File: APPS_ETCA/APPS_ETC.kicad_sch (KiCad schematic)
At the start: 7 parts, among them U1 NUCLEO-L432KC, U2 ISO1050DUB, U3 A1365xKTTN-1, U4 A1365xKTTN-1, U5 L78S05CV

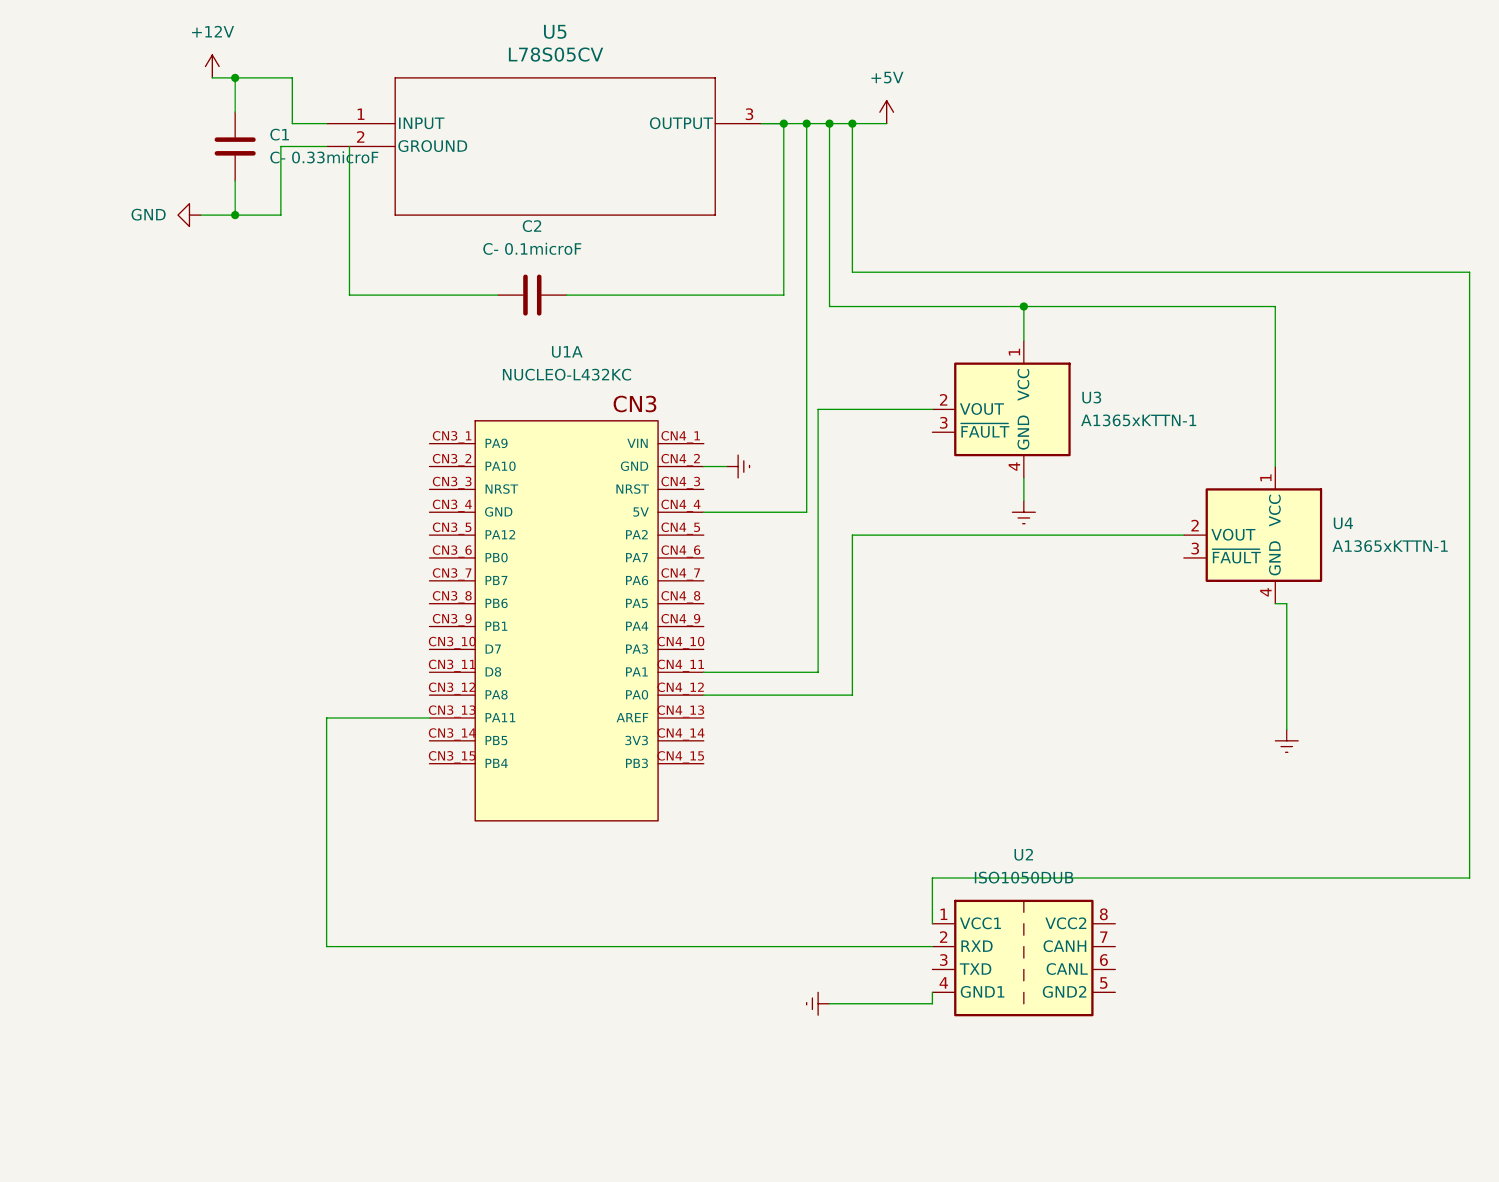
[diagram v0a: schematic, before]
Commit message: schema 3/4 done - need connectors in place of HE
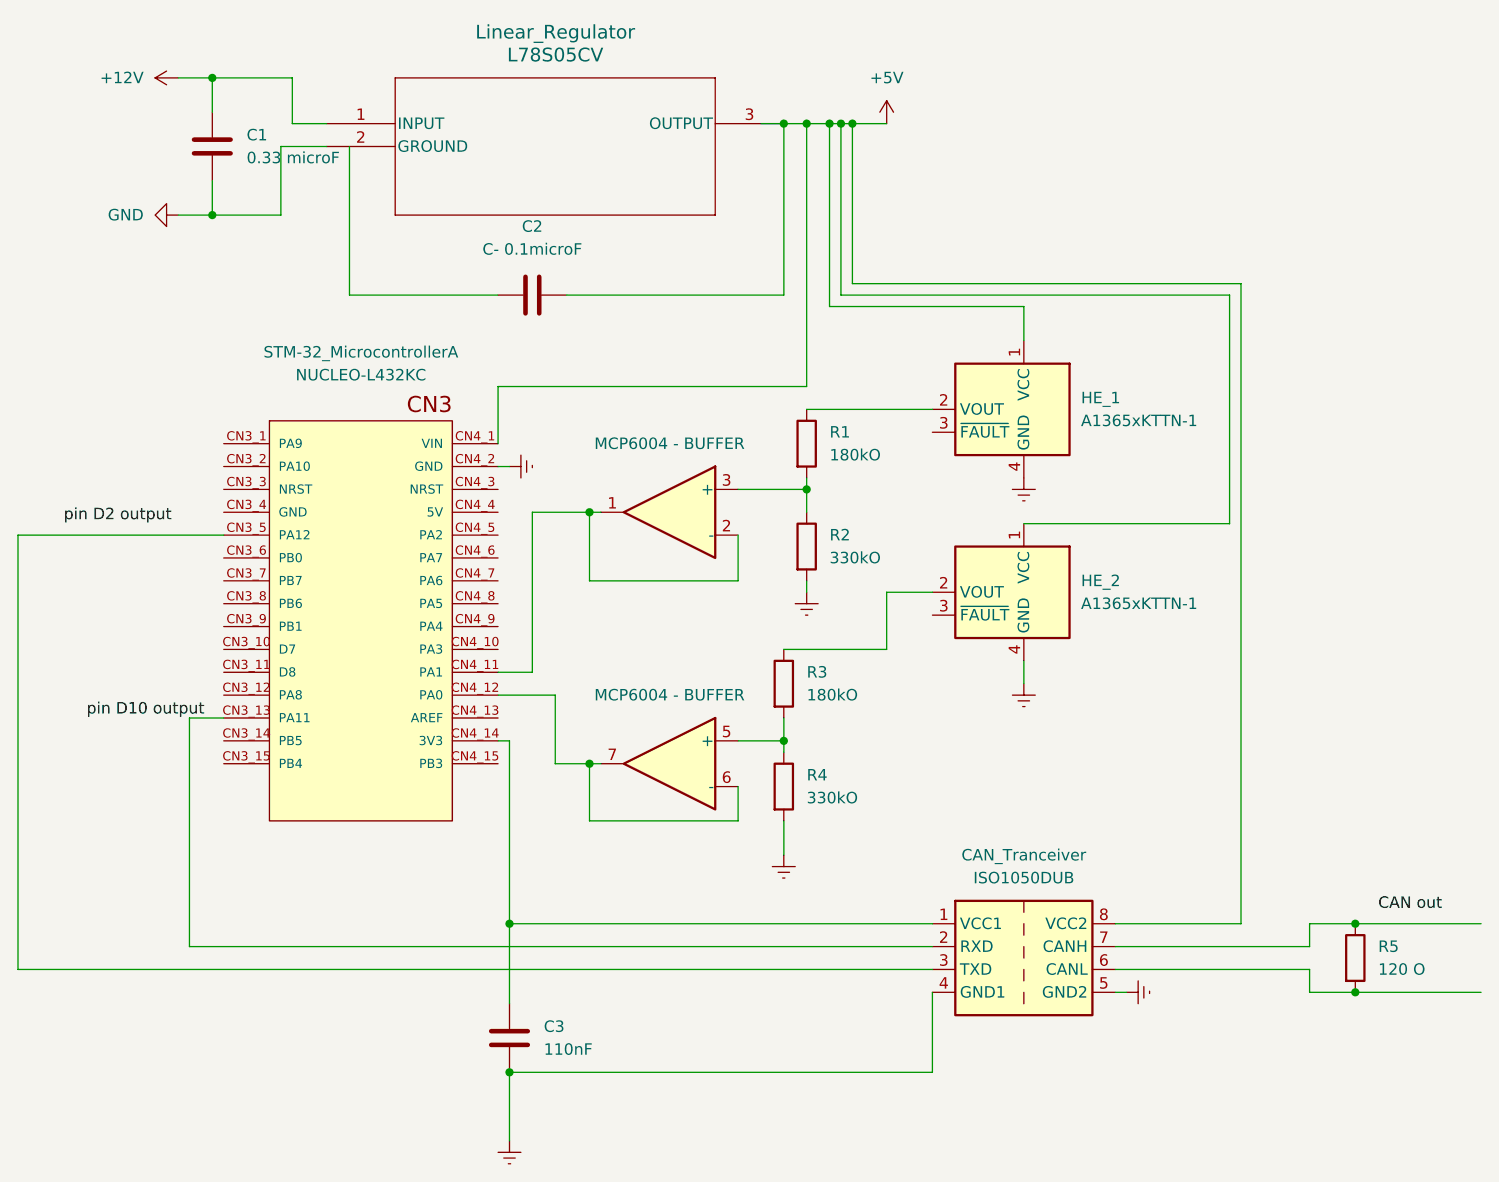
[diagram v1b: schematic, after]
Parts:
- added C3: 110nF, symbol Device:C
- added R1, R3: 180kO, symbol Device:R
- added R2, R4: 330kO, symbol Device:R
- added R5: 120 O, symbol Device:R
- added U6: MCP6004 - BUFFER, symbol Amplifier_Operational:MCP6004
- C1: value C- 0.33microF -> 0.33 microF
- renumbered U2 to CAN_Tranceiver, U3 to HE_1, U4 to HE_2, U5 to Linear_Regulator, U1 to STM-32_Microcontroller
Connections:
- net +5V: now also CAN_Tranceiver.8 (VCC2), STM-32_Microcontroller.CN4_1 (VIN); no longer CAN_Tranceiver.1 (VCC1), STM-32_Microcontroller.CN4_4 (5V)
- net Earth: now also CAN_Tranceiver.5 (GND2), C3.2, R2.2, R4.2
- net at HE_1.2 (VOUT): now also R1.1; no longer STM-32_Microcontroller.CN4_11 (PA1)
- net at STM-32_Microcontroller.CN3_5 (PA12): now also CAN_Tranceiver.3 (TXD)
- net at HE_2.2 (VOUT): now also R3.1; no longer STM-32_Microcontroller.CN4_12 (PA0)
- net at STM-32_Microcontroller.CN4_14 (3V3): now also CAN_Tranceiver.1 (VCC1), C3.1
- net at CAN_Tranceiver.6 (CANL): now also R5.2
- net at CAN_Tranceiver.7 (CANH): now also R5.1
- new net: R3.2, R4.1, U6.5 (+)
- new net: STM-32_Microcontroller.CN4_12 (PA0), U6.6 (-), U6.7
- new net: R1.2, R2.1, U6.3 (+)
- new net: STM-32_Microcontroller.CN4_11 (PA1), U6.1, U6.2 (-)
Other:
- moved on the sheet: C1, HE_2, STM-32_MicrocontrollerA

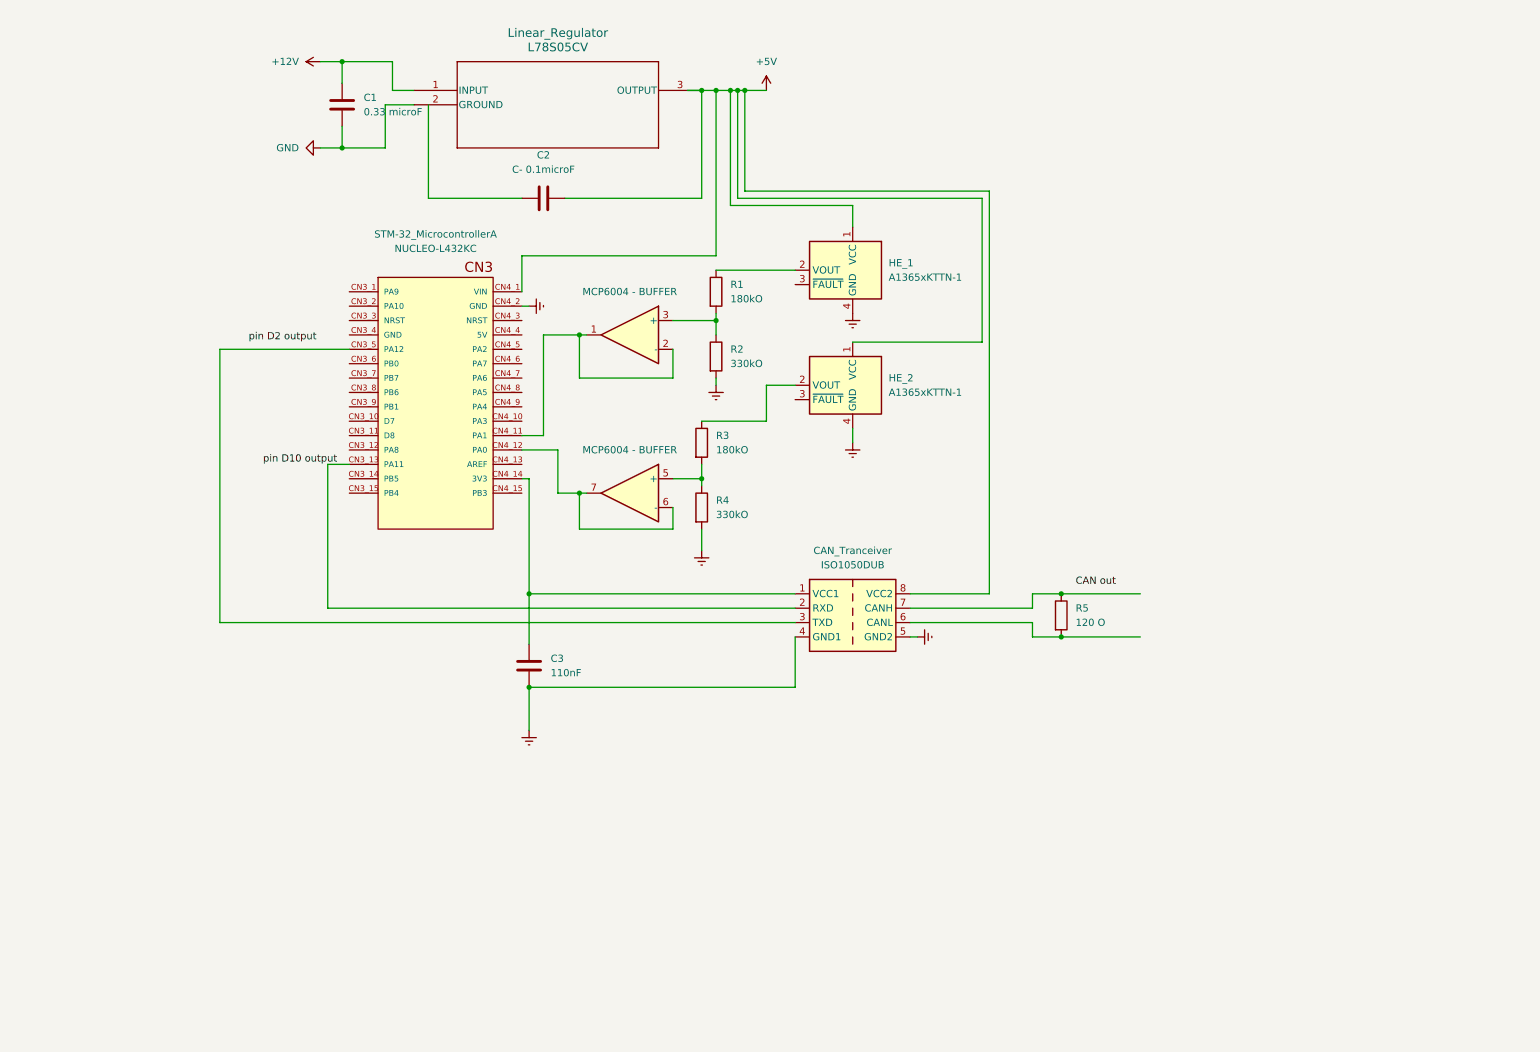
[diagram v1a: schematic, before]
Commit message: Added footprints for enclosure connector Add RTDS and TSAL Control Circuit. Add enclosure connections.
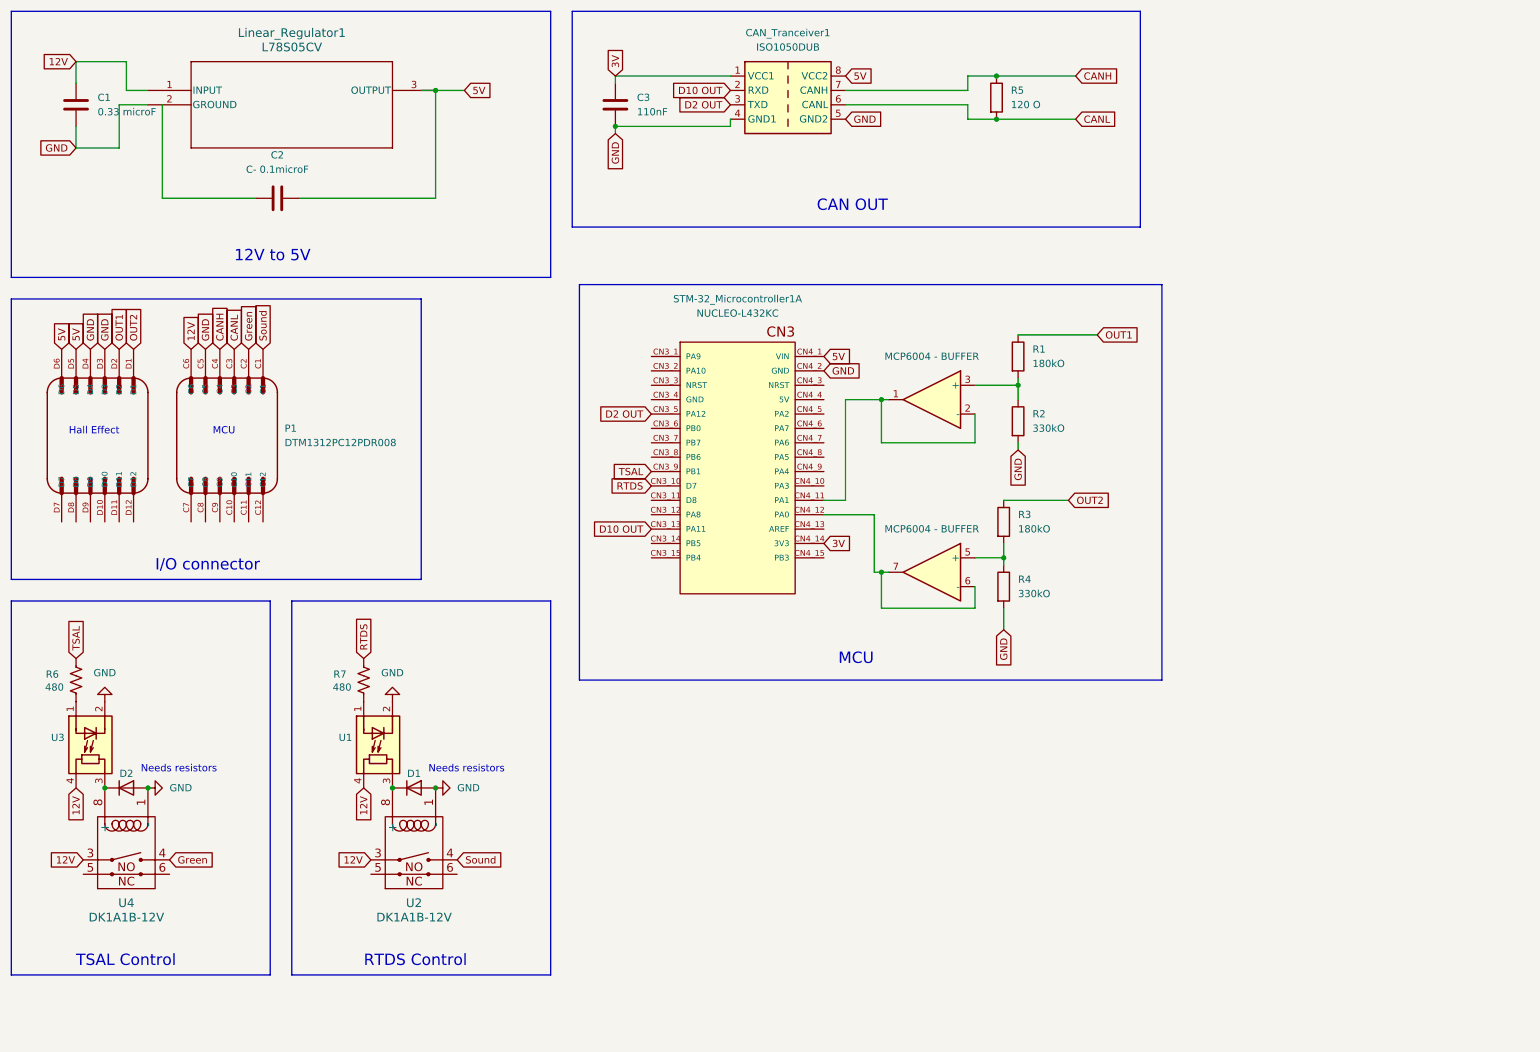
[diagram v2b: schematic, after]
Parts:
- removed HE_1, HE_2: A1365xKTTN-1, Sensor_Current:Allegro_SIP-4, symbol Sensor_Current:A1365xKTTN-1
- added D1, D2: D, Diode_THT:D_DO-41_SOD81_P10.16mm_Horizontal, symbol Device:D
- added P1: DTM1312PC12PDR008, DTM1312PC12PDR008:TE_DTM1312PC12PDR008, symbol 1FS_2_Global_Symbol_Library:DTM1312PC12PDR008
- added R6, R7: 480, Resistor_THT:R_Axial_DIN0207_L6.3mm_D2.5mm_P10.16mm_Horizontal, symbol Device:R_US
- added U1, U3: NSL-32, 1FS_2_Global_Footprint_Library:OptoCoupler 6-SOP, symbol Isolator:NSL-32
- added U2, U4: DK1A1B-12V, 1FS_2_Global_Footprint_Library:RELAY_DK2A_PAN, symbol 2FS-1_Symbol Library:DK1A1B-12V
- renumbered CAN_Tranceiver to CAN_Tranceiver1, Linear_Regulator to Linear_Regulator1, STM-32_Microcontroller to STM-32_Microcontroller1
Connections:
- net Earth is gone; now on net GND: C3.2, CAN_Tranceiver1.4 (GND1), CAN_Tranceiver1.5 (GND2), R2.2, R4.2, STM-32_Microcontroller1.CN4_2 (GND)
- net GND: now also D1.2 (A), D2.2 (A), P1.C5, P1.D3, P1.D4, U1.2 (K), U2.1 (-), U3.2 (K), U4.1 (-)
- net OUT2: now reaches R3.1
- net OUT2: now also P1.D1
- net CANH: now reaches CAN_Tranceiver1.7 (CANH), R5.1
- net CANH: now also P1.C4
- net CANL: now reaches CAN_Tranceiver1.6 (CANL), R5.2
- net CANL: now also P1.C3
- net 3V: now reaches C3.1, CAN_Tranceiver1.1 (VCC1), STM-32_Microcontroller1.CN4_14 (3V3)
- net OUT1: now reaches R1.1
- net OUT1: now also P1.D2
- net RTDS: now reaches STM-32_Microcontroller1.CN3_10 (D7)
- net RTDS: now also R7.2
- net D10 OUT: now reaches CAN_Tranceiver1.2 (RXD), STM-32_Microcontroller1.CN3_13 (PA11)
- net D2 OUT: now reaches CAN_Tranceiver1.3 (TXD), STM-32_Microcontroller1.CN3_5 (PA12)
- net TSAL: now reaches STM-32_Microcontroller1.CN3_9 (PB1)
- net TSAL: now also R6.2
- net +12V renamed 12V
- net 12V: now also P1.C6, U1.4 (R), U2.3, U3.4 (R), U4.3
- net +5V renamed 5V
- net 5V: now also P1.D5, P1.D6
- new net: R7.1, U1.1 (A)
- new net: D1.1 (K), U1.3 (R), U2.8 (+)
- new net: D2.1 (K), U3.3 (R), U4.8 (+)
- new net: R6.1, U3.1 (A)
- new net Green: P1.C2, U4.4
- new net Sound: P1.C1, U2.4
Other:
- note added: "12V to 5V"
- note added: "CAN OUT"
- note added: "Hall Effect"
- note added: "I/O connector"
- note added: "MCU"
- note added: "Needs resistors"
- note added: "RTDS Control"
- note added: "TSAL Control"
- title: (none) -> APPS/RTDS MCU PCB
- moved on the sheet: C1, C2, C3, CAN_Tranceiver1, Linear_Regulator1, R1, R2, R3, R4, R5, STM-32_Microcontroller1A
